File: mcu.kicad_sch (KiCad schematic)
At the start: 5 parts, among them IC1 TXU0101DCKR, J9 Conn_ARM_SWD_TagConnect_TC2030, U1 holyiot-21069

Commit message: Update
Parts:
- J9: value Conn_ARM_SWD_TagConnect_TC2030 -> Conn_ARM_SWD_TagConnect_TC2030_NL; footprint Connector:Tag-Connect_TC2030-IDC-FP_2x03_P1.27mm_Vertical -> Connector:Tag-Connect_TC2030-IDC-NL_2x03_P1.27mm_Vertical
- renumbered C60 to C62
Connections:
- net +3.3V renamed +3.3V_SYS
- net +5V renamed +5V_SYS
- net USB_DM_P renamed USB_DN_P
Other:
- moved on the sheet: C61
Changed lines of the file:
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@@
+	)
+	(junction
+		(at 200.66 135.89)
+		(diameter 0)
+		(color 0 0 0 0)
 	)
 	(junction
@@
 		(color 0 0 0 0)
 	)
-	(junction
-		(at 203.2 135.89)
-		(diameter 0)
-		(color 0 0 0 0)
-	)
 	(no_connect
 		(at 88.9 176.53)
@@
 	(wire
 		(pts
-			(xy 199.39 135.89) (xy 203.2 135.89)
+			(xy 196.85 135.89) (xy 200.66 135.89)
 		)
 		(stroke
@@
 	(wire
 		(pts
-			(xy 203.2 135.89) (xy 238.76 135.89)
-		)
-		(stroke
-			(width 0)
-			(type default)
-		)
-	)
-	(wire
-		(pts
 			(xy 237.49 149.86) (xy 237.49 148.59)
 		)
@@
 	(wire
 		(pts
-			(xy 203.2 135.89) (xy 203.2 142.24)
+			(xy 200.66 135.89) (xy 200.66 142.24)
 		)
 		(stroke
@@
 	(wire
 		(pts
+			(xy 200.66 135.89) (xy 238.76 135.89)
+		)
+		(stroke
+			(width 0)
+			(type default)
+		)
+	)
+	(wire
+		(pts
 			(xy 30.48 30.48) (xy 41.91 30.48)
 		)
@@
 		)
 	)
-	(label "USB_DM_P"
+	(label "USB_DN_P"
 		(at 86.36 152.4 0)
 		(effects
@@
 		(on_board yes)
 		(dnp no)
-		(fields_autoplaced yes)
 		(property "Reference" "#PWR034"
 			(at 86.36 179.07 0)
@@
 			)
 		)
-		(property "Value" "+3.3V"
-			(at 78.74 179.0699 90)
-			(effects
-				(font
-					(size 1.27 1.27)
-				)
-				(justify left)
+		(property "Value" "+3.3V_SYS"
+			(at 74.168 179.07 90)
+			(effects
+				(font
+					(size 1.27 1.27)
+				)
 			)
 		)
@@
 		(dnp no)
 		(fields_autoplaced yes)
-		(property "Reference" "C60"
+		(property "Reference" "C62"
 			(at 220.98 145.0339 0)
 			(effects
@@
 			(project "ykb-dactyl-v1"
 				(path "/e14fa40b-de41-4d68-adfe-82a50bad5819/8fdf36b3-219d-4291-9ca3-c54f1688288f"
-					(reference "C60")
+					(reference "C62")
 					(unit 1)
 				)
@@
 	(symbol
 		(lib_id "power:GND")
-		(at 203.2 149.86 0)
+		(at 200.66 149.86 0)
 		(unit 1)
 		(exclude_from_sim no)
@@
 		(fields_autoplaced yes)
 		(property "Reference" "#PWR048"
-			(at 203.2 156.21 0)
+			(at 200.66 156.21 0)
 			(effects
 				(font
@@
 		)
 		(property "Value" "GND"
-			(at 203.2 154.94 0)
+			(at 200.66 154.94 0)
 			(effects
 				(font
@@
 		)
 		(property "Footprint" ""
-			(at 203.2 149.86 0)
+			(at 200.66 149.86 0)
 			(effects
 				(font
@@
 		)
 		(property "Datasheet" ""
-			(at 203.2 149.86 0)
+			(at 200.66 149.86 0)
 			(effects
 				(font
@@
 		)
 		(property "Description" "Power symbol creates a global label with name \"GND\" , ground"
-			(at 203.2 149.86 0)
+			(at 200.66 149.86 0)
 			(effects
 				(font
@@
 			)
 		)
-		(property "Value" "+5V"
+		(property "Value" "+5V_SYS"
 			(at 210.82 138.4301 90)
 			(effects
@@
 		(on_board yes)
 		(dnp no)
-		(fields_autoplaced yes)
 		(property "Reference" "#PWR039"
 			(at 181.61 109.22 0)
@@
 			)
 		)
-		(property "Value" "+3.3V"
-			(at 176.53 106.68 90)
+		(property "Value" "+3.3V_SYS"
+			(at 169.164 109.22 90)
 			(effects
 				(font
@@
 	(symbol
 		(lib_id "Device:C_US")
-		(at 203.2 146.05 0)
+		(at 200.66 146.05 0)
 		(unit 1)
 		(exclude_from_sim no)
@@
 		(fields_autoplaced yes)
 		(property "Reference" "C61"
-			(at 207.01 145.0339 0)
+			(at 204.47 145.0339 0)
 			(effects
 				(font
@@
 		)
 		(property "Value" "0.1uF"
-			(at 207.01 147.5739 0)
+			(at 204.47 147.5739 0)
 			(effects
 				(font
@@
 		)
 		(property "Footprint" "Capacitor_SMD:C_0402_1005Metric"
-			(at 203.2 146.05 0)
+			(at 200.66 146.05 0)
 			(effects
 				(font
@@
 		)
 		(property "Datasheet" ""
-			(at 203.2 146.05 0)
+			(at 200.66 146.05 0)
 			(effects
 				(font
@@
 		)
 		(property "Description" "capacitor, US symbol"
-			(at 203.2 146.05 0)
+			(at 200.66 146.05 0)
 			(effects
 				(font
@@
 			)
 		)
-		(property "Value" "+5V"
+		(property "Value" "+5V_SYS"
 			(at 78.74 171.4501 90)
 			(effects
@@
 			)
 		)
-		(property "Value" "Conn_ARM_SWD_TagConnect_TC2030"
+		(property "Value" "Conn_ARM_SWD_TagConnect_TC2030_NL"
 			(at 201.93 116.8399 0)
 			(effects
@@
 			)
 		)
-		(property "Footprint" "Connector:Tag-Connect_TC2030-IDC-FP_2x03_P1.27mm_Vertical"
+		(property "Footprint" "Connector:Tag-Connect_TC2030-IDC-NL_2x03_P1.27mm_Vertical"
 			(at 191.516 140.462 0)
 			(effects
@@
 	(symbol
 		(lib_id "power:+3.3V")
-		(at 199.39 135.89 90)
+		(at 196.85 135.89 90)
 		(unit 1)
 		(exclude_from_sim no)
@@
 		(dnp no)
 		(property "Reference" "#PWR045"
-			(at 203.2 135.89 0)
-			(effects
-				(font
-					(size 1.27 1.27)
-				)
-				(hide yes)
-			)
-		)
-		(property "Value" "+3.3V"
-			(at 195.58 135.8899 90)
+			(at 200.66 135.89 0)
+			(effects
+				(font
+					(size 1.27 1.27)
+				)
+				(hide yes)
+			)
+		)
+		(property "Value" "+3.3V_SYS"
+			(at 193.04 135.8899 90)
 			(effects
 				(font
@@
 		)
 		(property "Footprint" ""
-			(at 199.39 135.89 0)
+			(at 196.85 135.89 0)
 			(effects
 				(font
@@
 		)
 		(property "Datasheet" ""
-			(at 199.39 135.89 0)
+			(at 196.85 135.89 0)
 			(effects
 				(font
@@
 		)
 		(property "Description" "Power symbol creates a global label with name \"+3.3V\""
-			(at 199.39 135.89 0)
-			(effects
-				(font
+			(at 196.85 135.89 0)
+			(effects
+				(font

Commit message: Update
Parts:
- added D1: QLS6B-FKW, LED_SMD:LED_Cree-PLCC6_4.7x1.5mm, symbol LED:QLS6B-FKW
- added R1, R2, R3: 1K, Resistor_SMD:R_0402_1005Metric, symbol Device:R_US
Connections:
- net +3.3V_SYS: now also D1.1 (AB), D1.3 (AR), D1.5 (AG)
- net SHDN: now reaches U1.P0.14
- net DBG_LED: now reaches U1.P0.15
- net DBG_LED: now also R3.1
- net BAT_STAT_1: now reaches U1.P0.17
- net BAT_STAT_1: now also R1.1
- net BAT_STAT_2: now reaches U1.P0.18
- net BAT_STAT_2: now also R2.1
- new net: D1.6 (KR), R2.2
- new net: D1.4 (KR), R1.2
- new net: D1.2 (KB), R3.2

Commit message: Update
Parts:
- removed J9: Conn_ARM_SWD_TagConnect_TC2030_NL, Connector:Tag-Connect_TC2030-IDC-NL_2x03_P1.27mm_Vertical, symbol Conn_ARM_SWD_TagConnect_TC2030-NL:Conn_ARM_SWD_TagConnect_TC2030
- added D2: QLS6B-FKW, LED_SMD:LED_Cree-PLCC6_4.7x1.5mm, symbol LED:QLS6B-FKW
- added J10, J9: Conn_01x05, Connector_PinSocket_2.54mm:PinSocket_1x05_P2.54mm_Vertical, symbol Connector_Generic:Conn_01x05
- added R4, R5, R6: 10K, Resistor_SMD:R_0402_1005Metric, symbol Device:R_US
- R1, R2, R3: value 1K -> 600
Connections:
- net +3.3V_SYS: now also D2.1 (AB), D2.3 (AR), D2.5 (AG), J10.1 (Pin_1), R4.2, R5.2, R6.2
- net BAT_STAT_1: now also R4.1
- net BAT_STAT_2: now also R5.1
- net DBG_LED: now also R6.1
- net DBG_UART_APPCORE_RX: now also J9.2 (Pin_2)
- net DBG_UART_APPCORE_TX: now also J9.1 (Pin_1)
- net DBG_UART_NETCORE_RX: now also J9.4 (Pin_4)
- net DBG_UART_NETCORE_TX: now also J9.3 (Pin_3)
- net GND: now also J10.5 (Pin_5), J9.5 (Pin_5)
- net RESET: now also J10.2 (Pin_2)
- net SWCLK: now also J10.3 (Pin_3)
- net SWDIO: now also J10.4 (Pin_4)
- net BAT_STAT_2_P: now reaches D1.6 (KR), R2.2
- net BAT_STAT_2_P: now also D2.6 (KR)
- net BAT_STAT_1_P: now reaches D1.4 (KR), R1.2
- net BAT_STAT_1_P: now also D2.4 (KR)
- net DBG_LED_P: now reaches D1.2 (KB), R3.2
- net DBG_LED_P: now also D2.2 (KB)
- net I2C_SCL: no longer names the net of U1.P1.4 (P1.04)
- net I2C_SDA: no longer names the net of U1.P1.2 (P1.02)
- no-connect marks 2 -> 1
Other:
- moved on the sheet: D1, R1, R2, R3

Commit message: Update
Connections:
- net SW_P: now reaches U1.P0.13
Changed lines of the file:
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@@
 	(generator_version "9.0")
 	(paper "A4")
+	(text_box "We have got 2 identical status LEDs on the board, this is for the symmetry purposes, only one of them is actually present depending on whether it is right or left variant."
+		(exclude_from_sim no)
+		(at 165.1 16.51 0)
+		(size 40.64 11.43)
+		(margins 0.9525 0.9525 0.9525 0.9525)
+		(stroke
+			(width 0)
+			(type solid)
+		)
+		(fill
+			(type none)
+		)
+		(effects
+			(font
+				(size 1.27 1.27)
+			)
+			(justify left top)
+		)
+	)
 	(text_box "When BQ25185 has 0 on VIN, is it ok to just have 3.3 pullup on BAT_STAT_1 and BAT_STAT_2?"
 		(exclude_from_sim no)
@@
 	(wire
 		(pts
+			(xy 33.02 53.34) (xy 41.91 53.34)
+		)
+		(stroke
+			(width 0)
+			(type default)
+		)
+	)
+	(wire
+		(pts
 			(xy 80.01 87.63) (xy 102.87 87.63)
 		)
@@
 		(effects
 			(font
+				(size 1.27 1.27)
+			)
+			(justify left bottom)
+		)
+	)
+	(label "SW_P"
+		(at 33.02 53.34 0)
+		(effects
+			(font

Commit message: Fix global nets
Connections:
- no-connect marks 1 -> 21

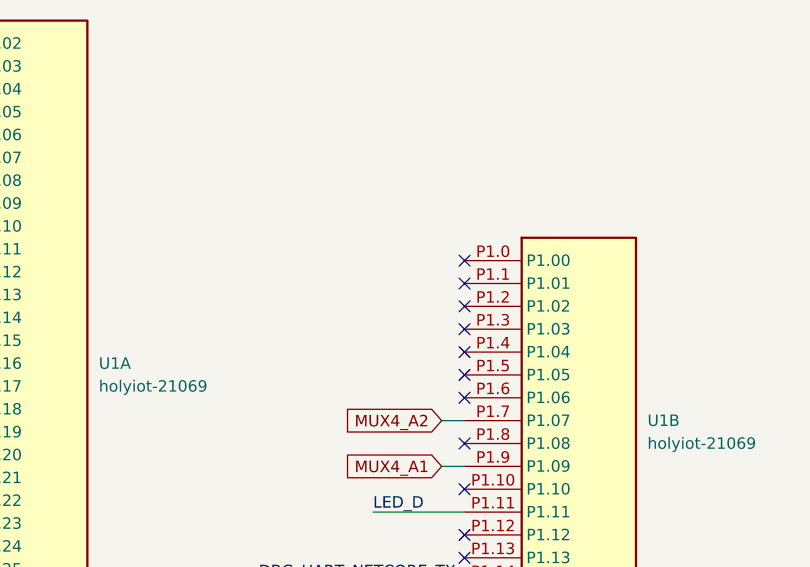
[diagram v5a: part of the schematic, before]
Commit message: Trace the board
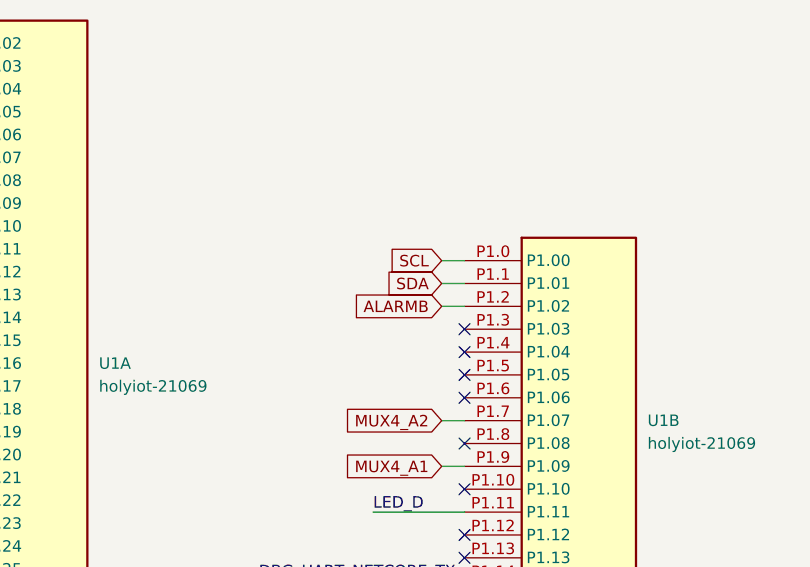
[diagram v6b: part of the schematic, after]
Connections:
- net SCL: now reaches U1.P1.0 (P1.00)
- net SDA: now reaches U1.P1.1 (P1.01)
- net ALARMB: now reaches U1.P1.2 (P1.02)
- no-connect marks 21 -> 18
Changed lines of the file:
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@@
-	)
-	(no_connect
-		(at 102.87 52.07)
 	)
 	(no_connect
@@
 	)
 	(no_connect
-		(at 102.87 54.61)
-	)
-	(no_connect
 		(at 41.91 60.96)
 	)
@@
 		(at 102.87 64.77)
 	)
-	(no_connect
-		(at 102.87 49.53)
-	)
 	(wire
 		(pts
@@
 	(wire
 		(pts
+			(xy 100.33 49.53) (xy 102.87 49.53)
+		)
+		(stroke
+			(width 0)
+			(type default)
+		)
+	)
+	(wire
+		(pts
 			(xy 38.1 68.58) (xy 41.91 68.58)
 		)
@@
 	(wire
 		(pts
+			(xy 100.33 54.61) (xy 102.87 54.61)
+		)
+		(stroke
+			(width 0)
+			(type default)
+		)
+	)
+	(wire
+		(pts
 			(xy 19.05 27.94) (xy 41.91 27.94)
 		)
@@
 		(pts
 			(xy 38.1 50.8) (xy 41.91 50.8)
+		)
+		(stroke
+			(width 0)
+			(type default)
+		)
+	)
+	(wire
+		(pts
+			(xy 100.33 52.07) (xy 102.87 52.07)
 		)
 		(stroke
@@
 			)
 			(justify left bottom)
+		)
+	)
+	(global_label "SDA"
+		(shape input)
+		(at 100.33 52.07 180)
+		(fields_autoplaced yes)
+		(effects
+			(font
+				(size 1.27 1.27)
+			)
+			(justify right)
+		)
+		(property "Intersheetrefs" "${INTERSHEET_REFS}"
+			(at 93.7767 52.07 0)
+			(effects
+				(font
+					(size 1.27 1.27)
+				)
+				(justify right)
+				(hide yes)
+			)
 		)
 	)
@@
 		)
 	)
+	(global_label "ALARMB"
+		(shape input)
+		(at 100.33 54.61 180)
+		(fields_autoplaced yes)
+		(effects
+			(font
+				(size 1.27 1.27)
+			)
+			(justify right)
+		)
+		(property "Intersheetrefs" "${INTERSHEET_REFS}"
+			(at 90.1481 54.61 0)
+			(effects
+				(font
+					(size 1.27 1.27)
+				)
+				(justify right)
+				(hide yes)
+			)
+		)
+	)
 	(global_label "SHDN"
 		(shape input)
@@
 				(hide yes)
 			)
+		)
+	)
+	(global_label "SCL"
+		(shape input)
+		(at 100.33 49.53 180)
+		(fields_autoplaced yes)
+		(effects
+			(font
+				(size 1.27 1.27)
+			)
+			(justify right)
+		)
+		(property "Intersheetrefs" "${INTERSHEET_REFS}"
+			(at 93.8372 49.53 0)
+			(effects
+				(font
+					(size 1.27 1.27)
+				)
+				(justify right)
+				(hide yes)
+			)

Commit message: Update
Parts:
- D2: now not fitted; now left out of the parts list
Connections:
- net CHARGER_EN: now reaches U1.P1.3 (P1.03)
- no-connect marks 18 -> 17
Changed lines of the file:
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@@
-	)
-	(no_connect
-		(at 102.87 57.15)
 	)
 	(no_connect
@@
 	(wire
 		(pts
+			(xy 100.33 57.15) (xy 102.87 57.15)
+		)
+		(stroke
+			(width 0)
+			(type default)
+		)
+	)
+	(wire
+		(pts
 			(xy 38.1 68.58) (xy 41.91 68.58)
 		)
@@
 		(property "Intersheetrefs" "${INTERSHEET_REFS}"
 			(at 93.7767 52.07 0)
+			(effects
+				(font
+					(size 1.27 1.27)
+				)
+				(justify right)
+				(hide yes)
+			)
+		)
+	)
+	(global_label "CHARGER_EN"
+		(shape input)
+		(at 100.33 57.15 180)
+		(fields_autoplaced yes)
+		(effects
+			(font
+				(size 1.27 1.27)
+			)
+			(justify right)
+		)
+		(property "Intersheetrefs" "${INTERSHEET_REFS}"
+			(at 85.2496 57.15 0)
 			(effects
 				(font
@@
 		(unit 1)
 		(exclude_from_sim no)
-		(in_bom yes)
+		(in_bom no)
 		(on_board yes)
-		(dnp no)
+		(dnp yes)
 		(property "Reference" "D2"
 			(at 181.61 53.34 0)

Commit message: Update
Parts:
- D1: now not fitted; now left out of the parts list
- D2: now fitted; now in the parts list
- J10, J9, U1: now left out of the parts list
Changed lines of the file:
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@@
 		(unit 2)
 		(exclude_from_sim no)
-		(in_bom yes)
+		(in_bom no)
 		(on_board yes)
 		(dnp no)
@@
 		(unit 1)
 		(exclude_from_sim no)
-		(in_bom no)
-		(on_board yes)
-		(dnp yes)
+		(in_bom yes)
+		(on_board yes)
+		(dnp no)
 		(property "Reference" "D2"
 			(at 181.61 53.34 0)
@@
 		(unit 1)
 		(exclude_from_sim no)
-		(in_bom yes)
+		(in_bom no)
 		(on_board yes)
 		(dnp no)
@@
 		(unit 3)
 		(exclude_from_sim no)
-		(in_bom yes)
+		(in_bom no)
 		(on_board yes)
 		(dnp no)
@@
 		(unit 4)
 		(exclude_from_sim no)
-		(in_bom yes)
+		(in_bom no)
 		(on_board yes)
 		(dnp no)
@@
 		(unit 5)
 		(exclude_from_sim no)
-		(in_bom yes)
+		(in_bom no)
 		(on_board yes)
 		(dnp no)
@@
 		(unit 1)
 		(exclude_from_sim no)
-		(in_bom yes)
+		(in_bom no)
 		(on_board yes)
 		(dnp no)
@@
 		(unit 1)
 		(exclude_from_sim no)
-		(in_bom yes)
+		(in_bom no)
 		(on_board yes)
 		(dnp no)
@@
 		(unit 1)
 		(exclude_from_sim no)
-		(in_bom yes)
-		(on_board yes)
-		(dnp no)
+		(in_bom no)
+		(on_board yes)
+		(dnp yes)
 		(fields_autoplaced yes)
 		(property "Reference" "D1"
